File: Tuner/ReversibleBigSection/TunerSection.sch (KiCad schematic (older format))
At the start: 118 parts, among them J1 Conn_01x03, J10 Conn_01x02, J11 Conn_02x05_Odd_Even, J12 Conn_01x01, J13 Conn_01x01, J14 Conn_01x01, J15 Conn_01x01, J16 Conn_01x01, J17 Conn_01x01, J18 Conn_01x01, J19 Conn_01x01, J2 Conn_01x03, J20 Conn_01x01, J21 Conn_01x01, J22 Conn_01x01, J3 Conn_01x03, J4 Conn_01x03, J5 Conn_01x03, J6 Conn_01x03, J7 Conn_01x03, J8 Conn_01x02, J9 Conn_01x02, P10 Conn_01x01, P11 Conn_01x01, P12 Conn_01x01, P2 Conn_01x01, P3 Conn_01x01, P4 Conn_01x01, P5 Conn_01x01, P6 Conn_01x01, P7 Conn_01x01, P8 Conn_01x01, P9 Conn_01x01, U1 MCP23008, U2 ULN2803A

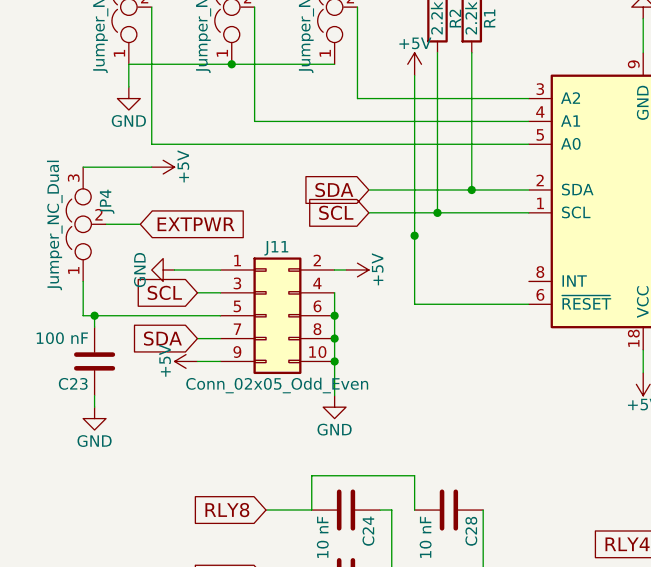
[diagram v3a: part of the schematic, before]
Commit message: Changed I2C cable pinoutgit add Tunergit add Tuner Also added ICOM rig support
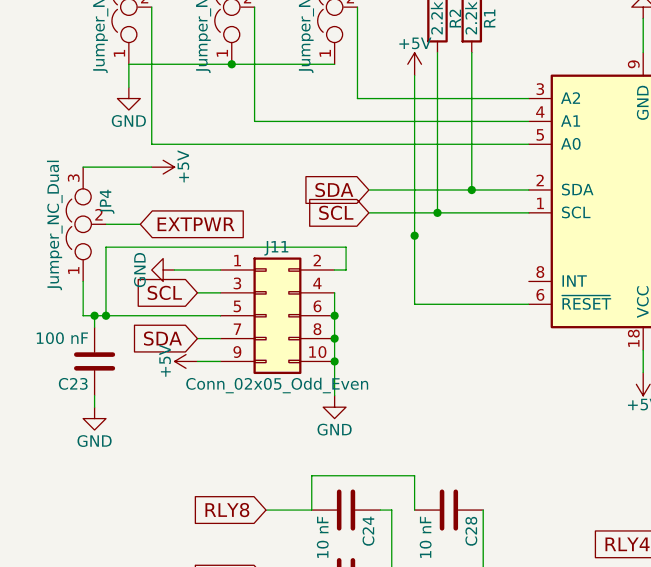
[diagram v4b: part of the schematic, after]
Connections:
- net +5V: no longer J11.2 (Pin_2)
- net at C23.2, J11.5 (Pin_5), JP4.1: now also J11.2 (Pin_2)
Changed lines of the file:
@@
-$EndComp
-$Comp
-L +5V #PWR014
-U 1 1 5BA4E273
-P 1850 5300
-F 0 "#PWR014" H 1850 5150 50  0001 C CNN
-F 1 "+5V" H 1850 5440 50  0000 C CNN
-F 2 "" H 1850 5300 50  0001 C CNN
-F 3 "" H 1850 5300 50  0001 C CNN
-	1    1850 5300
-	0    1    1    0
 $EndComp
 $Comp
@@
 	9750 3750 9900 3750
 Connection ~ 9900 3750
+Wire Wire Line
+	800  5500 800  5200
+Wire Wire Line
+	800  5200 1850 5200
+Wire Wire Line
+	1850 5200 1850 5300
+Connection ~ 800  5500
 $EndSCHEMATC

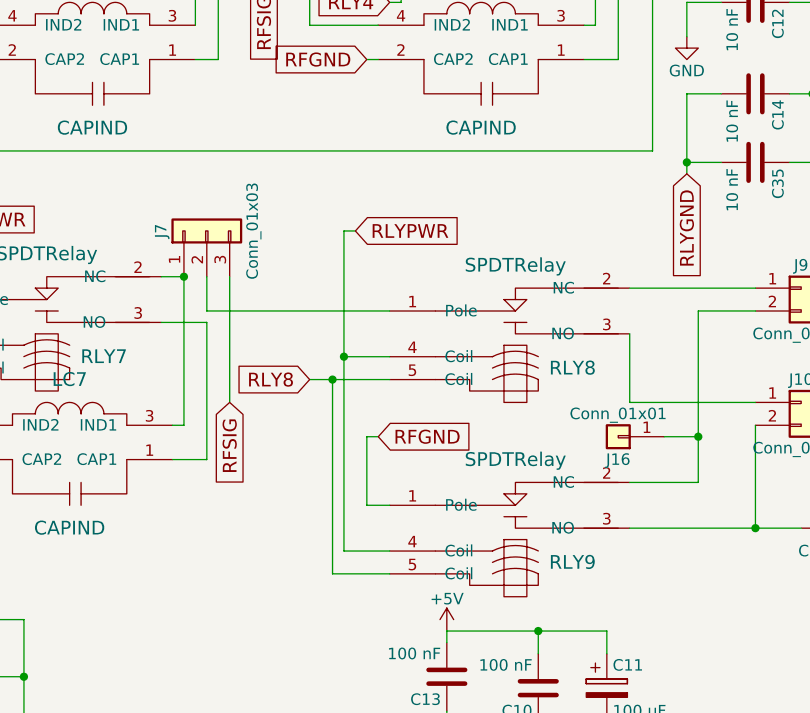
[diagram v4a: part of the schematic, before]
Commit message: Added nonswitched output to ReversibleSections
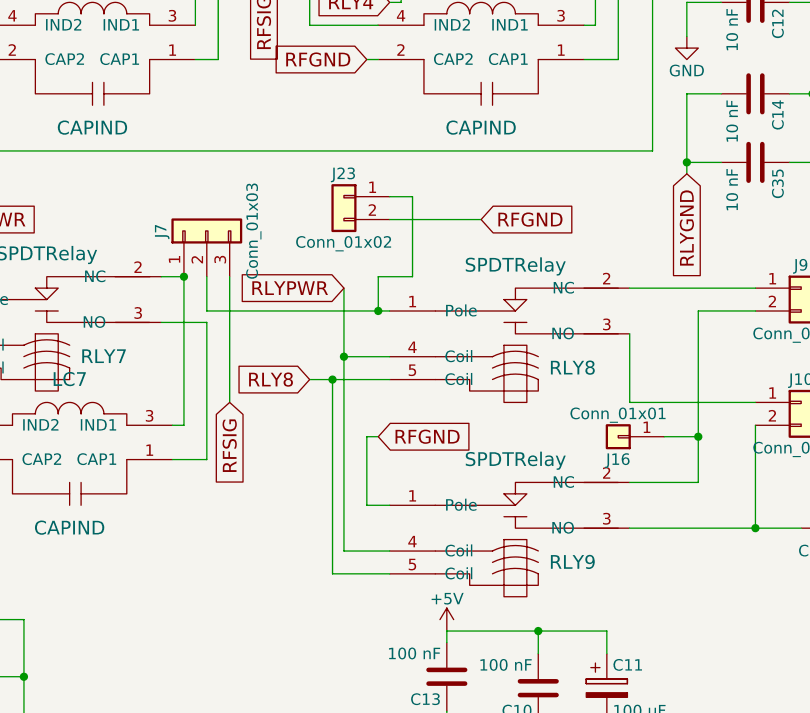
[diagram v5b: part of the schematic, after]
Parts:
- added J23: Conn_01x02, tuner:bnc_90_1-1337543-0_pad_combo, symbol Conn_01x02
- J10, J9: footprint tuner:bnc_90_1-1337543-0_pad_combo -> Connectors_Terminal_Blocks:TerminalBlock_bornier-2_P5.08mm
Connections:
- net RFGND: now also J23.2 (Pin_2)
- net at J7.2 (Pin_2), RLY8.1 (Pole): now also J23.1 (Pin_1)
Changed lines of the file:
@@
 F 0 "J10" H 10350 3700 50  0000 C CNN
 F 1 "Conn_01x02" H 10350 3400 50  0000 C CNN
-F 2 "tuner:bnc_90_1-1337543-0_pad_combo" H 10350 3600 50  0001 C CNN
+F 2 "Connectors_Terminal_Blocks:TerminalBlock_bornier-2_P5.08mm" H 10350 3600 50  0001 C CNN
 F 3 "" H 10350 3600 50  0001 C CNN
 	1    10350 3600
@@
 F 0 "J9" H 10350 3200 50  0000 C CNN
 F 1 "Conn_01x02" H 10350 2900 50  0000 C CNN
-F 2 "tuner:bnc_90_1-1337543-0_pad_combo" H 10350 3100 50  0001 C CNN
+F 2 "Connectors_Terminal_Blocks:TerminalBlock_bornier-2_P5.08mm" H 10350 3100 50  0001 C CNN
 F 3 "" H 10350 3100 50  0001 C CNN
 	1    10350 3100
@@
 Text GLabel 8500 3750 2    60   Input ~ 0
 RFGND
-$Comp
-L SPDTRelay RLY9
-U 1 1 5B18C0E7
-P 9100 4150
-F 0 "RLY9" H 9350 4000 60  0000 C CNN
-F 1 "SPDTRelay" H 9100 4450 60  0000 C CNN
-F 2 "tuner:SMIHRelay" H 9100 4150 60  0001 C CNN
-F 3 "" H 9100 4150 60  0001 C CNN
-	1    9100 4150
-	1    0    0    -1
-$EndComp
 $Comp
 L Conn_01x03 J7
@@
 Text GLabel 6550 2800 2    60   Input ~ 0
 RLYPWR
-Text GLabel 8400 2850 2    60   Input ~ 0
+Text GLabel 8350 3100 0    60   Input ~ 0
 RLYPWR
 Text GLabel 8300 1050 2    60   Input ~ 0
@@
 $EndComp
 $Comp
-L +5V #PWR015
+L +5V #PWR014
 U 1 1 5BA4E663
 P 1200 5700
-F 0 "#PWR015" H 1200 5550 50  0001 C CNN
+F 0 "#PWR014" H 1200 5550 50  0001 C CNN
 F 1 "+5V" H 1200 5840 50  0000 C CNN
 F 2 "" H 1200 5700 50  0001 C CNN
@@
 $EndComp
 $Comp
-L GND #PWR016
+L GND #PWR015
 U 1 1 5BA4FB25
 P 750 5900
-F 0 "#PWR016" H 750 5650 50  0001 C CNN
+F 0 "#PWR015" H 750 5650 50  0001 C CNN
 F 1 "GND" H 750 5750 50  0000 C CNN
 F 2 "" H 750 5900 50  0001 C CNN
@@
 $EndComp
 $Comp
-L GND #PWR017
+L GND #PWR016
 U 1 1 5BA5005D
 P 1100 5300
-F 0 "#PWR017" H 1100 5050 50  0001 C CNN
+F 0 "#PWR016" H 1100 5050 50  0001 C CNN
 F 1 "GND" H 1100 5150 50  0000 C CNN
 F 2 "" H 1100 5300 50  0001 C CNN
@@
 EXTPWR
 $Comp
-L +5V #PWR018
+L +5V #PWR017
 U 1 1 5BAE4DBC
 P 1000 4850
-F 0 "#PWR018" H 1000 4700 50  0001 C CNN
+F 0 "#PWR017" H 1000 4700 50  0001 C CNN
 F 1 "+5V" H 1000 4990 50  0000 C CNN
 F 2 "" H 1000 4850 50  0001 C CNN
@@
 $EndComp
 $Comp
-L GND #PWR019
+L GND #PWR018
 U 1 1 5BAEE216
 P 5050 7250
-F 0 "#PWR019" H 5050 7000 50  0001 C CNN
+F 0 "#PWR018" H 5050 7000 50  0001 C CNN
 F 1 "GND" H 5050 7100 50  0000 C CNN
 F 2 "" H 5050 7250 50  0001 C CNN
@@
 Wire Wire Line
 	8200 3500 8550 3500
-Connection ~ 8350 3400
 Wire Wire Line
 	8350 4250 8550 4250
 Wire Wire Line
 	8350 3400 8550 3400
-Wire Wire Line
-	8350 2850 8350 4250
 Connection ~ 9200 5000
 Connection ~ 9200 4600
@@
 Wire Wire Line
 	6450 2800 6550 2800
-Wire Wire Line
-	8400 2850 8350 2850
 Wire Wire Line
 	8300 1050 8250 1050
@@
 $EndComp
 Connection ~ 10150 4150
+Connection ~ 9900 3750
+Wire Wire Line
+	800  5500 800  5200
+Wire Wire Line
+	800  5200 1850 5200
+Wire Wire Line
+	1850 5200 1850 5300
+Connection ~ 800  5500
+Wire Wire Line
+	8350 3100 8350 4250
+$Comp
+L Conn_01x02 J23
+U 1 1 5C9BD7D9
+P 8350 2700
+F 0 "J23" H 8350 2800 50  0000 C CNN
+F 1 "Conn_01x02" H 8350 2500 50  0000 C CNN
+F 2 "tuner:bnc_90_1-1337543-0_pad_combo" H 8350 2700 50  0001 C CNN
+F 3 "" H 8350 2700 50  0001 C CNN
+	1    8350 2700
+	-1   0    0    -1
+$EndComp
+Text GLabel 8950 2800 2    60   Input ~ 0
+RFGND
+Wire Wire Line
+	8950 2800 8550 2800
+Wire Wire Line
+	8500 3200 8500 3050
+Wire Wire Line
+	8500 3050 8650 3050
+Wire Wire Line
+	8650 3050 8650 2700
+Wire Wire Line
+	8650 2700 8550 2700
+Connection ~ 8500 3200
+Wire Wire Line
+	9750 3750 9900 3750
 $Comp
 L Conn_01x01 J16
@@
 	-1   0    0    1
 $EndComp
-Wire Wire Line
-	9750 3750 9900 3750
-Connection ~ 9900 3750
-Wire Wire Line
-	800  5500 800  5200
-Wire Wire Line
-	800  5200 1850 5200
-Wire Wire Line
-	1850 5200 1850 5300
-Connection ~ 800  5500
+$Comp
+L SPDTRelay RLY9
+U 1 1 5B18C0E7
+P 9100 4150
+F 0 "RLY9" H 9350 4000 60  0000 C CNN
+F 1 "SPDTRelay" H 9100 4450 60  0000 C CNN
+F 2 "tuner:SMIHRelay" H 9100 4150 60  0001 C CNN
+F 3 "" H 9100 4150 60  0001 C CNN
+	1    9100 4150
+	1    0    0    -1
+$EndComp
+Connection ~ 8350 3400
 $EndSCHEMATC

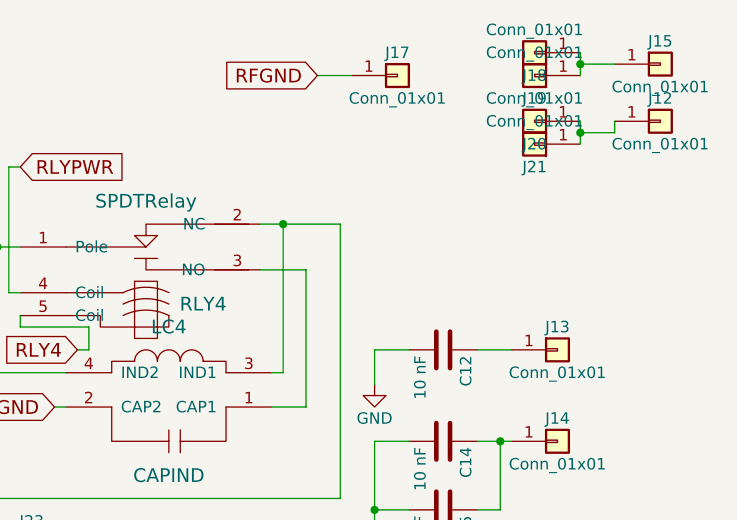
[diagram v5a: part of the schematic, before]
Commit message: Added extra capacitors between relay power and ground posts
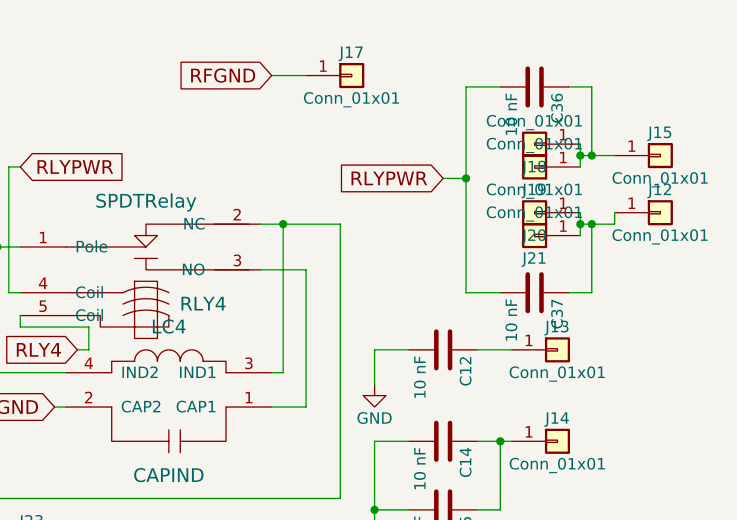
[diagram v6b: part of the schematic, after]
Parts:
- added C36, C37: 10 nF, Capacitors_THT:C_Disc_D5.0mm_W2.5mm_P2.50mm, symbol C
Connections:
- net RLYPWR: now also C36.2, C37.2
- net at J15.1 (Pin_1), J18.1 (Pin_1), J19.1 (Pin_1): now also C36.1
- net at J12.1 (Pin_1), J20.1 (Pin_1), J21.1 (Pin_1): now also C37.1
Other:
- moved on the sheet: J12, J15, J17, J18, J19, J20, J21
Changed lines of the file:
@@
 RLY8
 $Comp
-L +5V #PWR01
+L +5V #PWR12
 U 1 1 5B1A0287
 P 3150 5750
-F 0 "#PWR01" H 3150 5600 50  0001 C CNN
+F 0 "#PWR12" H 3150 5600 50  0001 C CNN
 F 1 "+5V" H 3150 5890 50  0000 C CNN
 F 2 "" H 3150 5750 50  0001 C CNN
@@
 $EndComp
 $Comp
-L GND #PWR02
+L GND #PWR3
 U 1 1 5B1AA0F6
 P 900 4500
-F 0 "#PWR02" H 900 4250 50  0001 C CNN
+F 0 "#PWR3" H 900 4250 50  0001 C CNN
 F 1 "GND" H 900 4350 50  0000 C CNN
 F 2 "" H 900 4500 50  0001 C CNN
@@
 $EndComp
 $Comp
-L +5V #PWR03
+L +5V #PWR2
 U 1 1 5B1AABE9
 P 900 3750
-F 0 "#PWR03" H 900 3600 50  0001 C CNN
+F 0 "#PWR2" H 900 3600 50  0001 C CNN
 F 1 "+5V" H 900 3890 50  0000 C CNN
 F 2 "" H 900 3750 50  0001 C CNN
@@
 $EndComp
 $Comp
-L +5V #PWR04
+L +5V #PWR8
 U 1 1 5B1ABA5A
 P 2150 4450
-F 0 "#PWR04" H 2150 4300 50  0001 C CNN
+F 0 "#PWR8" H 2150 4300 50  0001 C CNN
 F 1 "+5V" H 2150 4590 50  0000 C CNN
 F 2 "" H 2150 4450 50  0001 C CNN
@@
 $EndComp
 $Comp
-L +5V #PWR05
+L +5V #PWR10
 U 1 1 5B1ABCDE
 P 2400 3950
-F 0 "#PWR05" H 2400 3800 50  0001 C CNN
+F 0 "#PWR10" H 2400 3800 50  0001 C CNN
 F 1 "+5V" H 2400 4090 50  0000 C CNN
 F 2 "" H 2400 3950 50  0001 C CNN
@@
 $EndComp
 $Comp
-L +5V #PWR06
+L +5V #PWR16
 U 1 1 5B1ABFC6
 P 8800 4600
-F 0 "#PWR06" H 8800 4450 50  0001 C CNN
+F 0 "#PWR16" H 8800 4450 50  0001 C CNN
 F 1 "+5V" H 8800 4740 50  0000 C CNN
 F 2 "" H 8800 4600 50  0001 C CNN
@@
 $EndComp
 $Comp
-L GND #PWR07
+L GND #PWR17
 U 1 1 5B1AC04C
 P 8800 5050
-F 0 "#PWR07" H 8800 4800 50  0001 C CNN
+F 0 "#PWR17" H 8800 4800 50  0001 C CNN
 F 1 "GND" H 8800 4900 50  0000 C CNN
 F 2 "" H 8800 5050 50  0001 C CNN
@@
 L Conn_01x01 J15
 U 1 1 5B19812D
-P 11100 600
-F 0 "J15" H 11100 700 50  0000 C CNN
-F 1 "Conn_01x01" H 11100 500 50  0000 C CNN
-F 2 "Connectors:1pin" H 11100 600 50  0001 C CNN
-F 3 "" H 11100 600 50  0001 C CNN
-	1    11100 600
+P 11100 1000
+F 0 "J15" H 11100 1100 50  0000 C CNN
+F 1 "Conn_01x01" H 11100 900 50  0000 C CNN
+F 2 "Connectors:1pin" H 11100 1000 50  0001 C CNN
+F 3 "" H 11100 1000 50  0001 C CNN
+	1    11100 1000
 	1    0    0    -1
 $EndComp
@@
 L Conn_01x01 J12
 U 1 1 5B1981D8
-P 11100 850
-F 0 "J12" H 11100 950 50  0000 C CNN
-F 1 "Conn_01x01" H 11100 750 50  0000 C CNN
-F 2 "Connectors:1pin" H 11100 850 50  0001 C CNN
-F 3 "" H 11100 850 50  0001 C CNN
-	1    11100 850
+P 11100 1250
+F 0 "J12" H 11100 1350 50  0000 C CNN
+F 1 "Conn_01x01" H 11100 1150 50  0000 C CNN
+F 2 "Connectors:1pin" H 11100 1250 50  0001 C CNN
+F 3 "" H 11100 1250 50  0001 C CNN
+	1    11100 1250
 	1    0    0    -1
 $EndComp
@@
 $EndComp
 $Comp
-L +5V #PWR08
+L +5V #PWR9
 U 1 1 5B196BCE
 P 2250 3950
-F 0 "#PWR08" H 2250 3800 50  0001 C CNN
+F 0 "#PWR9" H 2250 3800 50  0001 C CNN
 F 1 "+5V" H 2250 4090 50  0000 C CNN
 F 2 "" H 2250 3950 50  0001 C CNN
@@
 $EndComp
 $Comp
-L GND #PWR09
+L GND #PWR14
 U 1 1 5B9A4AE1
 P 4850 6650
-F 0 "#PWR09" H 4850 6400 50  0001 C CNN
+F 0 "#PWR14" H 4850 6400 50  0001 C CNN
 F 1 "GND" H 4850 6500 50  0000 C CNN
 F 2 "" H 4850 6650 50  0001 C CNN
@@
 $EndComp
 $Comp
-L GND #PWR010
+L GND #PWR11
 U 1 1 5B9A6036
 P 3150 4200
-F 0 "#PWR010" H 3150 3950 50  0001 C CNN
+F 0 "#PWR11" H 3150 3950 50  0001 C CNN
 F 1 "GND" H 3150 4050 50  0000 C CNN
 F 2 "" H 3150 4200 50  0001 C CNN
@@
 $EndComp
 $Comp
-L GND #PWR011
+L GND #PWR13
 U 1 1 5B9ACA36
 P 3550 6100
-F 0 "#PWR011" H 3550 5850 50  0001 C CNN
+F 0 "#PWR13" H 3550 5850 50  0001 C CNN
 F 1 "GND" H 3550 5950 50  0000 C CNN
 F 2 "" H 3550 6100 50  0001 C CNN
@@
 $EndComp
 $Comp
-L GND #PWR012
+L GND #PWR18
 U 1 1 5B982525
 P 9850 2000
-F 0 "#PWR012" H 9850 1750 50  0001 C CNN
+F 0 "#PWR18" H 9850 1750 50  0001 C CNN
 F 1 "GND" H 9850 1850 50  0000 C CNN
 F 2 "" H 9850 2000 50  0001 C CNN
@@
 $EndComp
 $Comp
-L GND #PWR013
+L GND #PWR7
 U 1 1 5BA4D8F3
 P 1800 5850
-F 0 "#PWR013" H 1800 5600 50  0001 C CNN
+F 0 "#PWR7" H 1800 5600 50  0001 C CNN
 F 1 "GND" H 1800 5700 50  0000 C CNN
 F 2 "" H 1800 5850 50  0001 C CNN
@@
 $EndComp
 $Comp
-L +5V #PWR014
+L +5V #PWR6
 U 1 1 5BA4E663
 P 1200 5700
-F 0 "#PWR014" H 1200 5550 50  0001 C CNN
+F 0 "#PWR6" H 1200 5550 50  0001 C CNN
 F 1 "+5V" H 1200 5840 50  0000 C CNN
 F 2 "" H 1200 5700 50  0001 C CNN
@@
 $EndComp
 $Comp
-L GND #PWR015
+L GND #PWR1
 U 1 1 5BA4FB25
 P 750 5900
-F 0 "#PWR015" H 750 5650 50  0001 C CNN
+F 0 "#PWR1" H 750 5650 50  0001 C CNN
 F 1 "GND" H 750 5750 50  0000 C CNN
 F 2 "" H 750 5900 50  0001 C CNN
@@
 $EndComp
 $Comp
-L GND #PWR016
+L GND #PWR5
 U 1 1 5BA5005D
 P 1100 5300
-F 0 "#PWR016" H 1100 5050 50  0001 C CNN
+F 0 "#PWR5" H 1100 5050 50  0001 C CNN
 F 1 "GND" H 1100 5150 50  0000 C CNN
 F 2 "" H 1100 5300 50  0001 C CNN
@@
 EXTPWR
 $Comp
-L +5V #PWR017
+L +5V #PWR4
 U 1 1 5BAE4DBC
 P 1000 4850
-F 0 "#PWR017" H 1000 4700 50  0001 C CNN
+F 0 "#PWR4" H 1000 4700 50  0001 C CNN
 F 1 "+5V" H 1000 4990 50  0000 C CNN
 F 2 "" H 1000 4850 50  0001 C CNN
@@
 $EndComp
 $Comp
-L GND #PWR018
+L GND #PWR15
 U 1 1 5BAEE216
 P 5050 7250
-F 0 "#PWR018" H 5050 7000 50  0001 C CNN
+F 0 "#PWR15" H 5050 7000 50  0001 C CNN
 F 1 "GND" H 5050 7100 50  0000 C CNN
 F 2 "" H 5050 7250 50  0001 C CNN
@@
 	0    1    1    0
 $EndComp
-Text GLabel 9600 650  0    60   Input ~ 0
+Text GLabel 9400 650  0    60   Input ~ 0
 RFGND
 $Comp
 L Conn_01x01 J17
 U 1 1 5BD84E29
-P 9950 650
-F 0 "J17" H 9950 750 50  0000 C CNN
-F 1 "Conn_01x01" H 9950 550 50  0000 C CNN
-F 2 "tuner:SOLDERJUMPER" H 9950 650 50  0001 C CNN
-F 3 "" H 9950 650 50  0001 C CNN
-	1    9950 650
+P 9750 650
+F 0 "J17" H 9750 750 50  0000 C CNN
+F 1 "Conn_01x01" H 9750 550 50  0000 C CNN
+F 2 "tuner:SOLDERJUMPER" H 9750 650 50  0001 C CNN
+F 3 "" H 9750 650 50  0001 C CNN
+	1    9750 650
 	1    0    0    -1
 $EndComp
@@
 Connection ~ 10400 2250
 Wire Wire Line
-	9750 650  9600 650
+	9550 650  9400 650
 $Comp
 L Conn_01x01 J18
 U 1 1 5BD85A19
-P 10550 550
-F 0 "J18" H 10550 650 50  0000 C CNN
-F 1 "Conn_01x01" H 10550 450 50  0000 C CNN
-F 2 "tuner:SOLDERJUMPER" H 10550 550 50  0001 C CNN
-F 3 "" H 10550 550 50  0001 C CNN
-	1    10550 550
-	-1   0    0    1
-$EndComp
-$Comp
-L Conn_01x01 J19
-U 1 1 5BD85C02
-P 10550 650
-F 0 "J19" H 10550 750 50  0000 C CNN
-F 1 "Conn_01x01" H 10550 550 50  0000 C CNN
-F 2 "tuner:SOLDERJUMPER" H 10550 650 50  0001 C CNN
-F 3 "" H 10550 650 50  0001 C CNN
-	1    10550 650
-	-1   0    0    1
-$EndComp
-Wire Wire Line
-	10750 550  10750 650
-Wire Wire Line
-	10750 600  10900 600
-Connection ~ 10750 600
-$Comp
-L Conn_01x01 J20
-U 1 1 5BD861F6
-P 10550 850
-F 0 "J20" H 10550 950 50  0000 C CNN
-F 1 "Conn_01x01" H 10550 750 50  0000 C CNN
-F 2 "tuner:SOLDERJUMPER" H 10550 850 50  0001 C CNN
-F 3 "" H 10550 850 50  0001 C CNN
-	1    10550 850
-	-1   0    0    1
-$EndComp
-$Comp
-L Conn_01x01 J21
-U 1 1 5BD86365
 P 10550 950
-F 0 "J21" H 10550 1050 50  0000 C CNN
+F 0 "J18" H 10550 1050 50  0000 C CNN
 F 1 "Conn_01x01" H 10550 850 50  0000 C CNN
 F 2 "tuner:SOLDERJUMPER" H 10550 950 50  0001 C CNN
@@
 	-1   0    0    1
 $EndComp
-Wire Wire Line
-	10750 850  10750 950
-Wire Wire Line
-	10900 850  10900 900
-Wire Wire Line
-	10900 900  10750 900
-Connection ~ 10750 900
+$Comp
+L Conn_01x01 J19
+U 1 1 5BD85C02
+P 10550 1050
+F 0 "J19" H 10550 1150 50  0000 C CNN
+F 1 "Conn_01x01" H 10550 950 50  0000 C CNN
+F 2 "tuner:SOLDERJUMPER" H 10550 1050 50  0001 C CNN
+F 3 "" H 10550 1050 50  0001 C CNN
+	1    10550 1050
+	-1   0    0    1
+$EndComp
+Wire Wire Line
+	10750 950  10750 1050
+Wire Wire Line
+	10750 1000 10900 1000
+Connection ~ 10750 1000
+$Comp
+L Conn_01x01 J20
+U 1 1 5BD861F6
+P 10550 1250
+F 0 "J20" H 10550 1350 50  0000 C CNN
+F 1 "Conn_01x01" H 10550 1150 50  0000 C CNN
+F 2 "tuner:SOLDERJUMPER" H 10550 1250 50  0001 C CNN
+F 3 "" H 10550 1250 50  0001 C CNN
+	1    10550 1250
+	-1   0    0    1
+$EndComp
+$Comp
+L Conn_01x01 J21
+U 1 1 5BD86365
+P 10550 1350
+F 0 "J21" H 10550 1450 50  0000 C CNN
+F 1 "Conn_01x01" H 10550 1250 50  0000 C CNN
+F 2 "tuner:SOLDERJUMPER" H 10550 1350 50  0001 C CNN
+F 3 "" H 10550 1350 50  0001 C CNN
+	1    10550 1350
+	-1   0    0    1
+$EndComp
+Wire Wire Line
+	10750 1250 10750 1350
+Wire Wire Line
+	10900 1250 10900 1300
+Wire Wire Line
+	10900 1300 10750 1300
+Connection ~ 10750 1300
 $Comp
 L Conn_01x01 J22
@@
 $EndComp
 Connection ~ 8350 3400
+Text GLabel 10150 1100 0    60   Input ~ 0
+RLYPWR
+$Comp
+L C C36
+U 1 1 5DDBD75D
+P 10550 700
+F 0 "C36" H 10575 800 50  0000 L CNN
+F 1 "10 nF" H 10575 600 50  0000 L CNN
+F 2 "Capacitors_THT:C_Disc_D5.0mm_W2.5mm_P2.50mm" H 10588 550 50  0001 C CNN
+F 3 "" H 10550 700 50  0001 C CNN
+	1    10550 700
+	0    1    1    0
+$EndComp
+Wire Wire Line
+	10150 1100 10250 1100
+Wire Wire Line
+	10250 700  10250 1600
+Wire Wire Line
+	10250 700  10400 700
+Wire Wire Line
+	10700 700  10800 700
+Wire Wire Line
+	10800 700  10800 1000
+Connection ~ 10800 1000
+$Comp
+L C C37
+U 1 1 5DDBDF54
+P 10550 1600
+F 0 "C37" H 10575 1700 50  0000 L CNN
+F 1 "10 nF" H 10575 1500 50  0000 L CNN
+F 2 "Capacitors_THT:C_Disc_D5.0mm_W2.5mm_P2.50mm" H 10588 1450 50  0001 C CNN
+F 3 "" H 10550 1600 50  0001 C CNN
+	1    10550 1600
+	0    1    1    0
+$EndComp
+Wire Wire Line
+	10250 1600 10400 1600
+Connection ~ 10250 1100
+Wire Wire Line
+	10700 1600 10800 1600
+Wire Wire Line
+	10800 1600 10800 1300
+Connection ~ 10800 1300
 $EndSCHEMATC

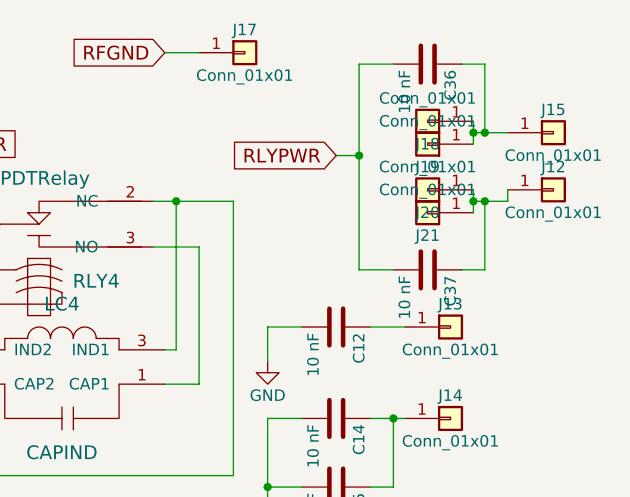
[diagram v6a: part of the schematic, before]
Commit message: Changed some of the capacitors to NC becaue they might cause problems in some situations
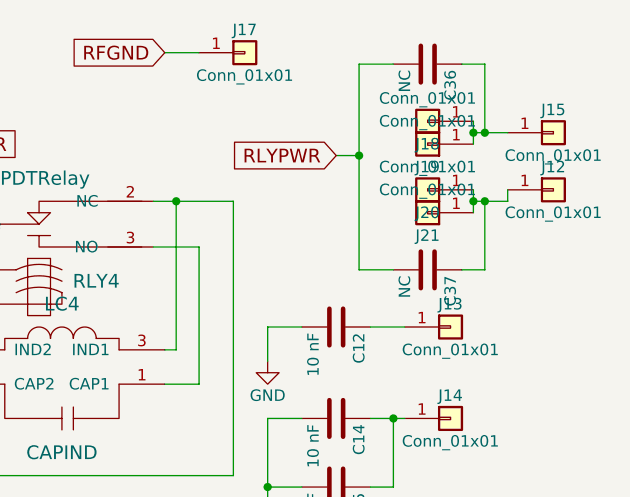
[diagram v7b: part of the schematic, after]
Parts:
- C36, C37: value 10 nF -> NC
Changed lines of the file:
@@
 P 10550 700
 F 0 "C36" H 10575 800 50  0000 L CNN
-F 1 "10 nF" H 10575 600 50  0000 L CNN
+F 1 "NC" H 10575 600 50  0000 L CNN
 F 2 "Capacitors_THT:C_Disc_D5.0mm_W2.5mm_P2.50mm" H 10588 550 50  0001 C CNN
 F 3 "" H 10550 700 50  0001 C CNN
@@
 P 10550 1600
 F 0 "C37" H 10575 1700 50  0000 L CNN
-F 1 "10 nF" H 10575 1500 50  0000 L CNN
+F 1 "NC" H 10575 1500 50  0000 L CNN
 F 2 "Capacitors_THT:C_Disc_D5.0mm_W2.5mm_P2.50mm" H 10588 1450 50  0001 C CNN
 F 3 "" H 10550 1600 50  0001 C CNN
